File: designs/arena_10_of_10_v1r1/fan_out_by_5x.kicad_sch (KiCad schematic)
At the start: 17 parts

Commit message: Added initial annotation.
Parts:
- gave numbers to parts that had none: 11

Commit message: Finished footprint assignment.
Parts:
- R28, R29, R30, R31, R32: footprint (none) -> Resistor_SMD:R_0402_1005Metric
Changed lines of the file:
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@@
 			)
 		)
-		(property "Footprint" ""
+		(property "Footprint" "Resistor_SMD:R_0402_1005Metric"
 			(at 91.44 72.39 0)
 			(effects
@@
 			)
 		)
-		(property "Footprint" ""
+		(property "Footprint" "Resistor_SMD:R_0402_1005Metric"
 			(at 91.44 105.41 0)
 			(effects
@@
 			)
 		)
-		(property "Footprint" ""
+		(property "Footprint" "Resistor_SMD:R_0402_1005Metric"
 			(at 91.44 39.37 0)
 			(effects
@@
 			)
 		)
-		(property "Footprint" ""
+		(property "Footprint" "Resistor_SMD:R_0402_1005Metric"
 			(at 91.44 55.88 0)
 			(effects
@@
 			)
 		)
-		(property "Footprint" ""
+		(property "Footprint" "Resistor_SMD:R_0402_1005Metric"
 			(at 91.44 88.9 0)
 			(effects

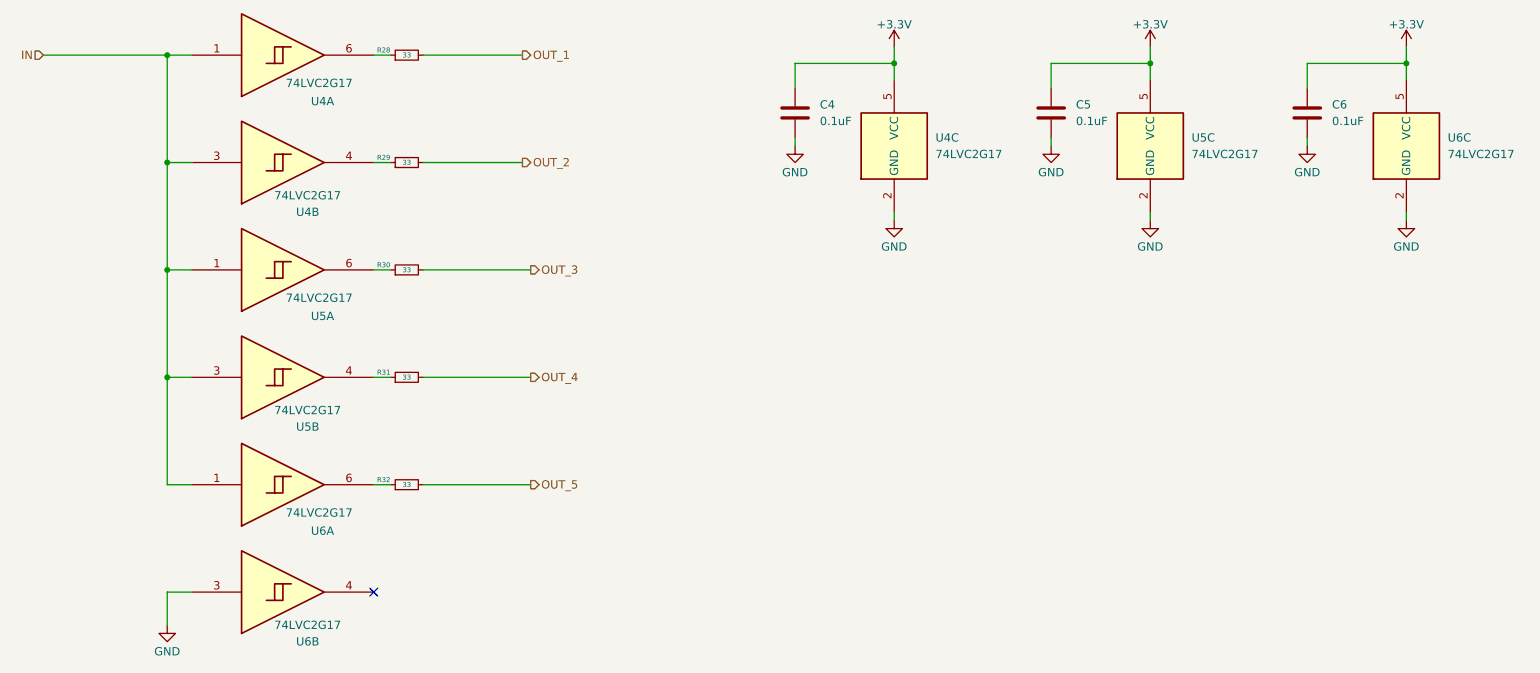
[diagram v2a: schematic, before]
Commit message: Resolved all DSR voilations in schematic.
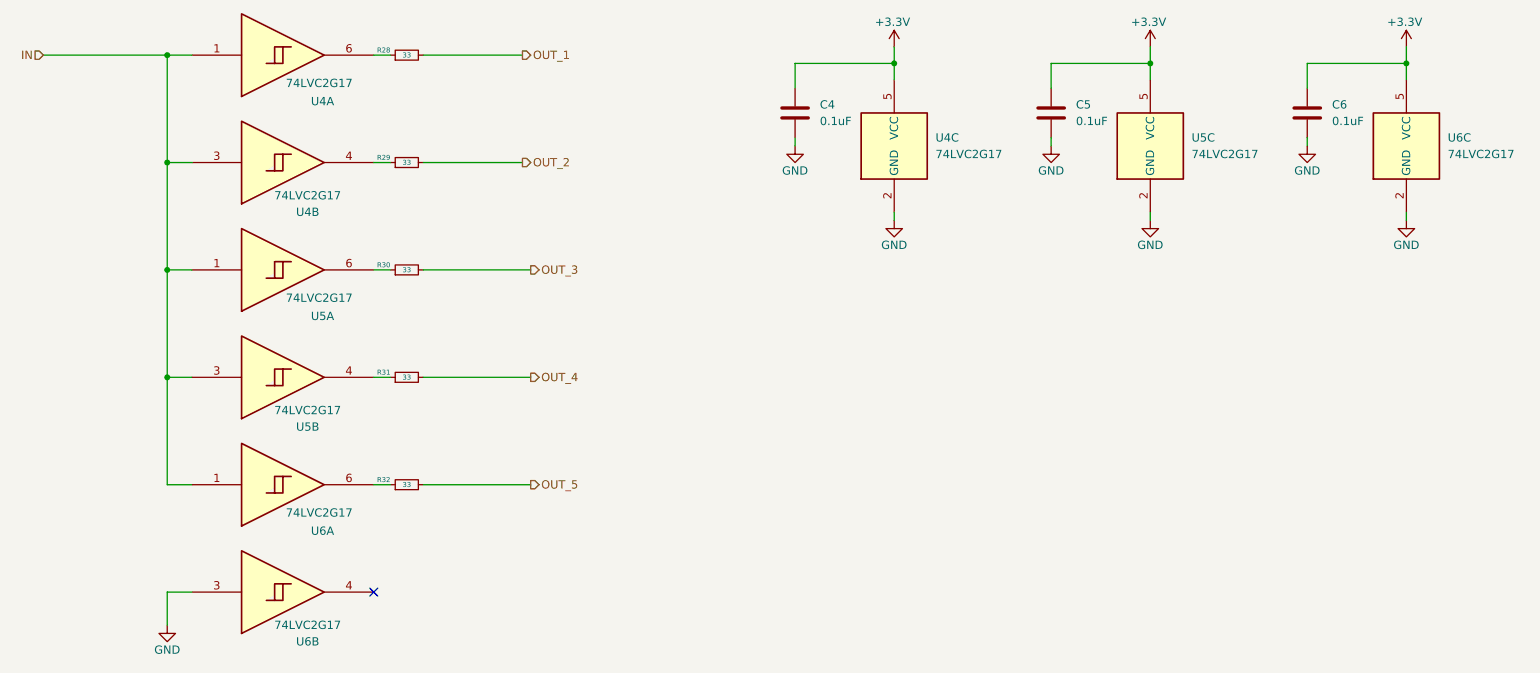
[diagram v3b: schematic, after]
